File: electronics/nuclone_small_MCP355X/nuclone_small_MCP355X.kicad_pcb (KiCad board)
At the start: 2 copper layers, 50 x 50 mm, 54 parts, among them J3 nuclone_small_left, J4 nuclone_small_right, J5 FTDI_PINS_1X06, J6 DevBoardUartInput

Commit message: WIP schematic, added breadboard, initial placement
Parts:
- added C1: 10n, SquantorRcl:C_0603, F.Cu at (85.0, 81.6)
- added C2: 2.2n, SquantorRcl:C_0603, F.Cu at (87.6, 81.6)
- added C3: 2.2n, SquantorRcl:C_0603, F.Cu at (82.4, 81.6)
- added C5: 1u, SquantorRcl:C_0603, F.Cu at (81.4, 74.8)
- added C6: 1u, SquantorRcl:C_0603, F.Cu at (81.4, 77.5)
- added D2: SD05, SquantorDiodes:SOD-323-nexperia-hand, F.Cu at (76.6, 106.9)
- added D3: SD05, SquantorDiodes:SOD-323-nexperia-hand, F.Cu at (76.6, 108.7)
- added D4: SD05, SquantorDiodes:SOD-323-nexperia-hand, F.Cu at (93.4, 108.7)
- added D5: SD05, SquantorDiodes:SOD-323-nexperia-hand, F.Cu at (93.4, 106.9)
- added J1: Conn_01x04, SquantorConnectors:Header-0254-1X04-H010, F.Cu at (81.2, 88.5)
- added J10: Conn_01x04, SquantorConnectors:Header-0254-1X04-H010, F.Cu at (83.7, 98.6)
- added J11: Conn_01x04, SquantorConnectors:Header-0254-1X04-H010, F.Cu at (86.3, 98.6)
- added J12: Conn_01x04, SquantorConnectors:Header-0254-1X04-H010, F.Cu at (88.8, 98.6)
- added J13: Conn_01x04, Connector_JST:JST_XH_B4B-XH-A_1x04_P2.50mm_Vertical, F.Cu at (81.2, 106.9)
- added J2: Conn_01x04, SquantorConnectors:Header-0254-1X04-H010, F.Cu at (83.7, 88.5)
- added J7: Conn_01x04, SquantorConnectors:Header-0254-1X04-H010, F.Cu at (86.3, 88.5)
- added J8: Conn_01x04, SquantorConnectors:Header-0254-1X04-H010, F.Cu at (88.8, 88.5)
- added J9: Conn_01x04, SquantorConnectors:Header-0254-1X04-H010, F.Cu at (81.2, 98.6)
- added R1: 1K, SquantorRcl:R_0603_hand, F.Cu at (83.7, 81.6)
- added R10: 1K, SquantorRcl:R_0805+0603, F.Cu at (93.3, 89.7)
- added R11: 1K, SquantorRcl:R_0805+0603, F.Cu at (93.0, 92.2)
- added R2: 1K, SquantorRcl:R_0603_hand, F.Cu at (86.3, 81.6)
- added R3: 100, SquantorRcl:R_0603_hand, F.Cu at (81.4, 72.0)
- added R4: 1K, SquantorRcl:R_0805+0603, F.Cu at (78.0, 84.7)
- added R5: 1K, SquantorRcl:R_0805+0603, F.Cu at (78.0, 87.2)
- added R6: 1K, SquantorRcl:R_0805+0603, F.Cu at (78.0, 89.8)
- added R7: 1K, SquantorRcl:R_0805+0603, F.Cu at (78.0, 92.2)
- added R8: 1K, SquantorRcl:R_0805+0603, F.Cu at (93.5, 86.9)
- added R9: 1K, SquantorRcl:R_0805+0603, F.Cu at (93.0, 84.7)
- added TP40: SCK, SquantorTestPoints:TestPoint_hole_H05R10_2side, F.Cu at (87.2, 71.5)
- added TP41: SDO, SquantorTestPoints:TestPoint_hole_H05R10_2side, F.Cu at (85.7, 71.5)
- added TP42: CS, SquantorTestPoints:TestPoint_hole_H05R10_2side, F.Cu at (84.2, 71.5)
- added U1: MCP355X-E_SN, SquantorIC:SOIC-8, F.Cu at (85.0, 76.1)
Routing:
- net /VDD2: track 7.48 -> 29.0 mm
- net /Input2: track 0.00 -> 19.0 mm
- net /Input3: track 0.00 -> 19.0 mm
- net /Input4: track 0.00 -> 15.7 mm
- net /Input1: track 0.00 -> 15.7 mm
- net /V_IN-: track 0.00 -> 11.2 mm
- net /V_IN+: track 0.00 -> 9.83 mm
- net Net-(U1-Vin+): track 0.00 -> 5.08 mm
- net Net-(U1-Vin-): track 0.00 -> 3.74 mm
- net Net-(U1-Vdd): track 0.00 -> 3.27 mm
- net /VREF: track 0.00 -> 3.06 mm
- net /SCK: track 0.00 -> 2.02 mm
- net /CS: track 0.00 -> 1.97 mm
- net /SDO: track 0.00 -> 1.93 mm
- net /VSS: vias 10 -> 15

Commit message: placing and silk placement
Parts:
- moved R9 2.66 mm to (92.1, 87.2)
- moved R8 2.61 mm to (92.1, 84.7)
- moved R10 1.20 mm to (92.1, 89.8)
- moved R11 0.90 mm to (92.1, 92.2)
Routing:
- net /VREF: track 3.06 -> 56.0 mm, vias 0 -> 2
- net /DIV3: track 0.00 -> 7.56 mm
- net /DIV4: track 0.00 -> 7.49 mm
- net /DIV1: track 0.00 -> 7.36 mm
- net /DIV2: track 0.00 -> 7.29 mm
- net /VSS: track 0.00 -> 4.84 mm, vias 15 -> 19

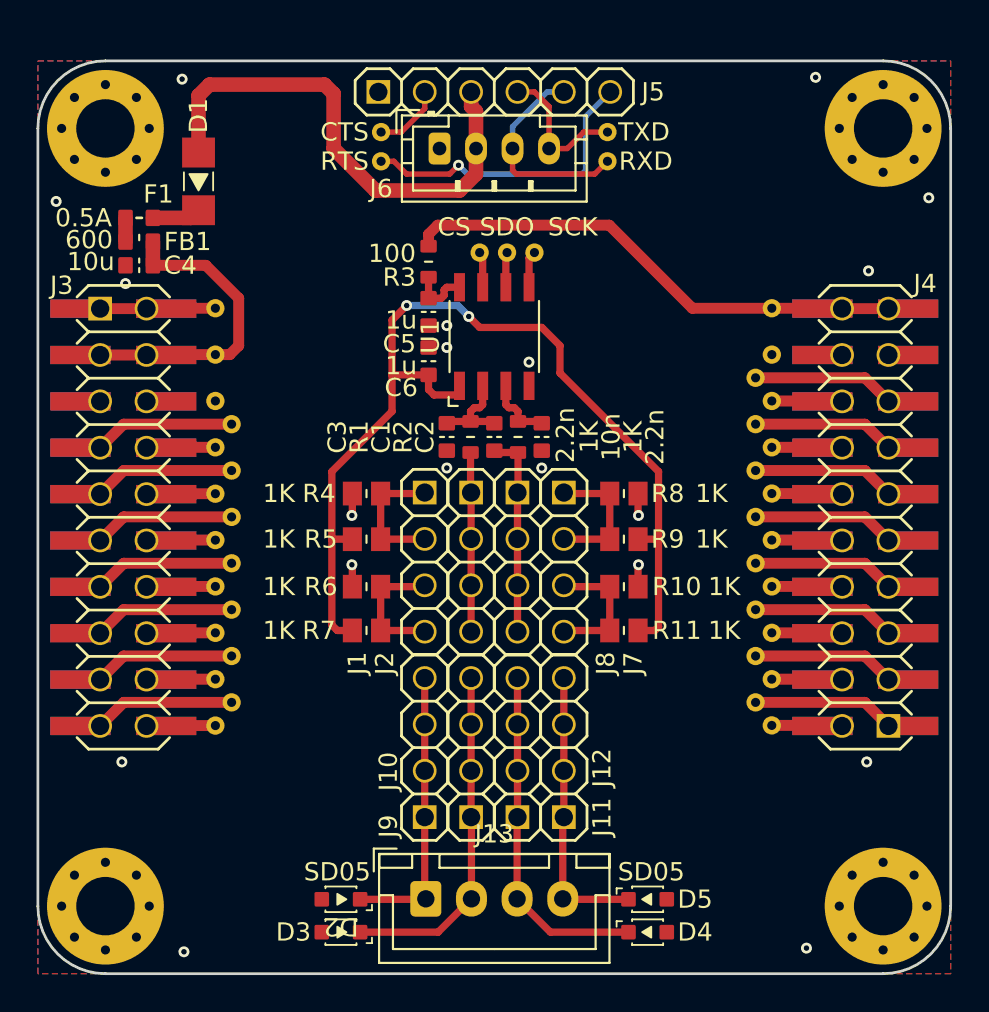
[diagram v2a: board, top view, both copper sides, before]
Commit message: added Voltage reference, placed and routed
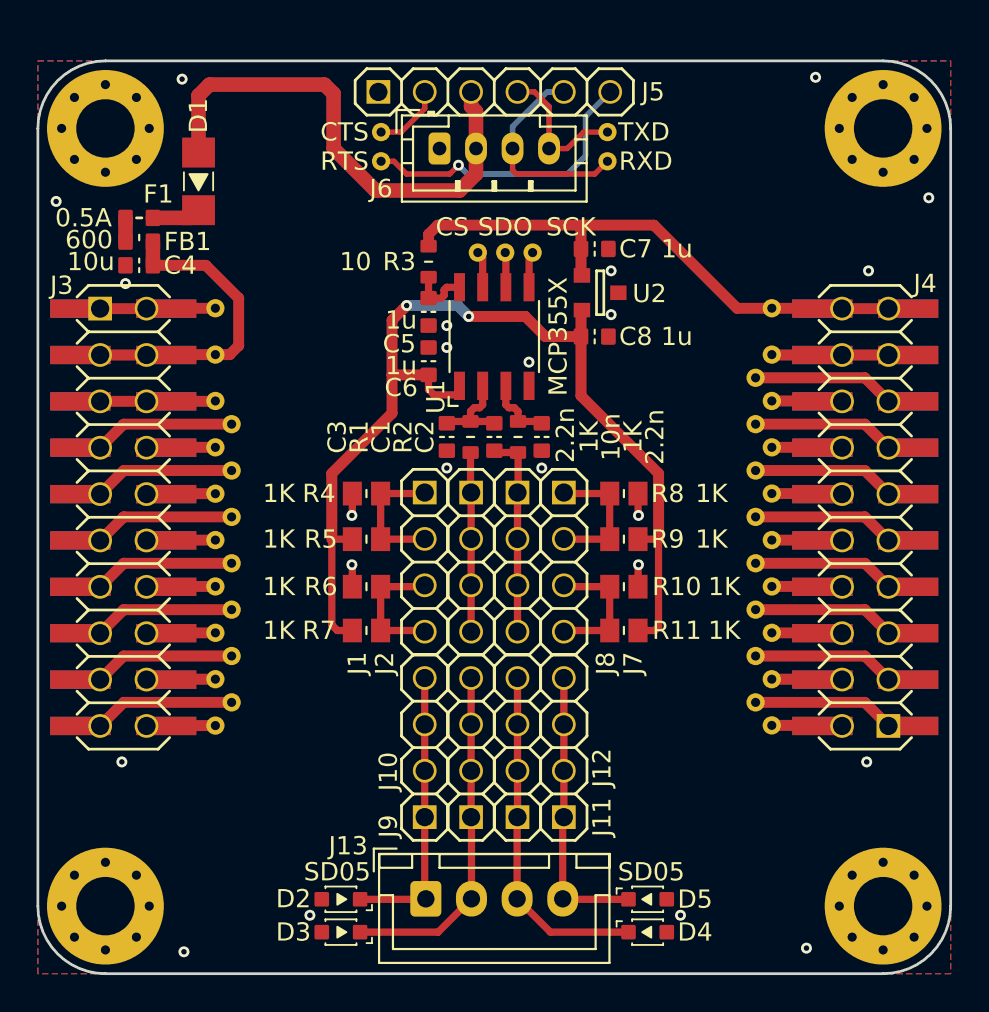
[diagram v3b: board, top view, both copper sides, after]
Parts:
- added C7: 1u, SquantorRcl:C_0603, F.Cu at (90.5, 71.3)
- added C8: 1u, SquantorRcl:C_0603, F.Cu at (90.5, 76.1)
- added U2: reference_sot23-3, SquantorIC:SOT23-3, F.Cu at (90.8, 73.7)
- N2: value V20230714 -> V20230801
- R3: value 100 -> 10
- U1: value MCP355X-E_SN -> MCP355X
- moved TP40 0.10 mm to (87.1, 71.5)
- moved TP41 0.10 mm to (85.6, 71.5)
- moved TP42 0.10 mm to (84.1, 71.5)
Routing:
- net /VSS: track 4.84 -> 18.6 mm, vias 19 -> 23
- net /VDD2: track 29.0 -> 31.8 mm
- net /VREF: track 56.0 -> 58.4 mm

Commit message: reviewed and small modifications
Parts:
- removed TP40: SCK, SquantorTestPoints:TestPoint_hole_H05R10_2side
- removed TP41: SDO, SquantorTestPoints:TestPoint_hole_H05R10_2side
- removed TP42: CS, SquantorTestPoints:TestPoint_hole_H05R10_2side
- added J14: Conn_01x03, SquantorConnectors:Header-0254-1X03-H010, F.Cu at (85.7, 70.8)
- N2: value V20230801 -> V20230915
- moved R3 1.92 mm to (80.2, 70.5)
- moved C7 0.70 mm to (91.2, 71.3)
- moved C8 0.70 mm to (91.2, 76.1)
- moved U2 0.70 mm to (91.5, 73.7)
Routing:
- net Net-(U1-Vdd): track 3.27 -> 5.27 mm
- net /SCK: track 1.98 -> 3.14 mm
- net /CS: track 2.01 -> 3.12 mm
- net /VDD2: track 31.8 -> 32.7 mm
- net /SDO: track 1.91 -> 2.61 mm

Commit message: updated changes and library
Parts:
- removed J14: Conn_01x03, SquantorConnectors:Header-0254-1X03-H010
- removed J5: FTDI_PINS_1X06, SquantorConnectors:Header-0254-1X06-H010
- removed TP36: CTS, SquantorTestPoints:TestPoint_hole_H05R10_2side
- removed TP37: RTS, SquantorTestPoints:TestPoint_hole_H05R10_2side
- removed TP38: TXD, SquantorTestPoints:TestPoint_hole_H05R10_2side
- removed TP39: RXD, SquantorTestPoints:TestPoint_hole_H05R10_2side
- added D6: LED, SquantorDiodes:LED_0603_hand, F.Cu at (71.2, 71.0)
- added J15: Conn_02x03_Odd_Even, SquantorConnectors:Header-0254-2X03-H010, F.Cu at (86.2, 74.4)
- added J16: Conn_02x04_Odd_Even, SquantorConnectors:Header-0254-2X04-H010, F.Cu at (93.4, 66.6)
- added R12: 1K, SquantorRcl:R_0603_hand, F.Cu at (68.3, 70.9)
- J10, J11, J12, J9: footprint SquantorConnectors:Header-0254-1X04-H010 -> SquantorConnectors:Header-0254-1X02-H010
- moved R3 7.12 mm to (80.7, 77.6), turned to 180 degrees
- moved C7 6.50 mm to (91.3, 77.8)
- moved C8 6.50 mm to (91.3, 82.6)
- moved U2 6.50 mm to (91.5, 80.2)
- moved R10 5.04 mm to (93.3, 94.7)
- moved R9 5.04 mm to (93.3, 92.1)
- moved R11 5.04 mm to (93.3, 97.1)
- moved R8 5.04 mm to (93.3, 89.6)
- moved R7 5.02 mm to (76.9, 97.1)
- moved R4 5.01 mm to (76.9, 89.6)
- moved R5 5.01 mm to (76.9, 92.1)
- moved R6 5.01 mm to (76.9, 94.7)
- moved C1 4.89 mm to (85.1, 86.5)
- moved C2 4.89 mm to (87.7, 86.5)
- moved C3 4.89 mm to (82.5, 86.5)
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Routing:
- net /RTS: track 16.4 -> 0.00 mm, vias 1 -> 0
- net /VIN: track 27.7 -> 19.0 mm
- net /Input1: track 15.7 -> 10.8 mm
- net /Input2: track 19.0 -> 14.1 mm
- net /Input4: track 15.7 -> 10.9 mm
- net /Input3: track 19.0 -> 14.1 mm
- net /VSS: track 18.6 -> 13.8 mm, vias 23 -> 22
- net /CTS: track 3.83 -> 0.00 mm
- net /DIV2: track 7.29 -> 9.67 mm
- net /DIV1: track 7.36 -> 9.74 mm
- net /DIV3: track 7.56 -> 9.79 mm
- net /DIV4: track 7.49 -> 9.70 mm
- net /VDD2: track 32.7 -> 34.8 mm, vias 0 -> 2
- net Net-(U1-Vdd): track 5.27 -> 3.43 mm
- net /RXD: track 11.6 -> 10.1 mm
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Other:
- board text added: "CS SDO SCK"
- board text added: "RXD TXD RTS CTS"

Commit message: updated versionnumber
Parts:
- N2: value V20230915 -> V20231203
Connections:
- J16 pad 1: /CTS -> unconnected-(J16-Pin_1-Pad1)
- J16 pad 3: /RTS -> unconnected-(J16-Pin_3-Pad3)
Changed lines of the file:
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@@
   (net 36 "/TXD")
   (net 37 "/RXD")
-  (net 38 "/RTS")
-  (net 39 "/CTS")
+  (net 38 "unconnected-(J16-Pin_1-Pad1)")
+  (net 39 "unconnected-(J16-Pin_3-Pad3)")
   (net 40 "Net-(D1-K)")
   (net 41 "/VIN")
@@
       (stroke (width 0.1) (type solid)) (fill solid) (layer "F.SilkS"))
     (pad "1" thru_hole roundrect (at -3.81 1.27 270) (size 1.4 1.4) (drill 1) (layers "*.Cu" "*.Mask") (roundrect_rratio 0.2)
-      (net 39 "/CTS") (pinfunction "Pin_1") (pintype "passive"))
+      (net 38 "unconnected-(J16-Pin_1-Pad1)") (pinfunction "Pin_1") (pintype "passive+no_connect"))
     (pad "2" thru_hole circle (at -3.81 -1.27) (size 1.4 1.4) (drill 1) (layers "*.Cu" "*.Mask")
       (net 2 "/VSS") (pinfunction "Pin_2") (pintype "passive"))
     (pad "3" thru_hole circle (at -1.27 1.27) (size 1.4 1.4) (drill 1) (layers "*.Cu" "*.Mask")
-      (net 38 "/RTS") (pinfunction "Pin_3") (pintype "passive"))
+      (net 39 "unconnected-(J16-Pin_3-Pad3)") (pinfunction "Pin_3") (pintype "passive+no_connect"))
     (pad "4" thru_hole circle (at -1.27 -1.27 270) (size 1.4 1.4) (drill 1) (layers "*.Cu" "*.Mask")
       (net 2 "/VSS") (pinfunction "Pin_4") (pintype "passive"))
@@
         (effects (font (size 1 1) (thickness 0.15)) (justify mirror))
     )
-    (fp_text value "V20230915" (at 0 0.1) (layer "B.SilkS")
+    (fp_text value "V20231203" (at 0 0.1) (layer "B.SilkS")
         (effects (font (size 0.8 0.8) (thickness 0.15)) (justify mirror))
     )

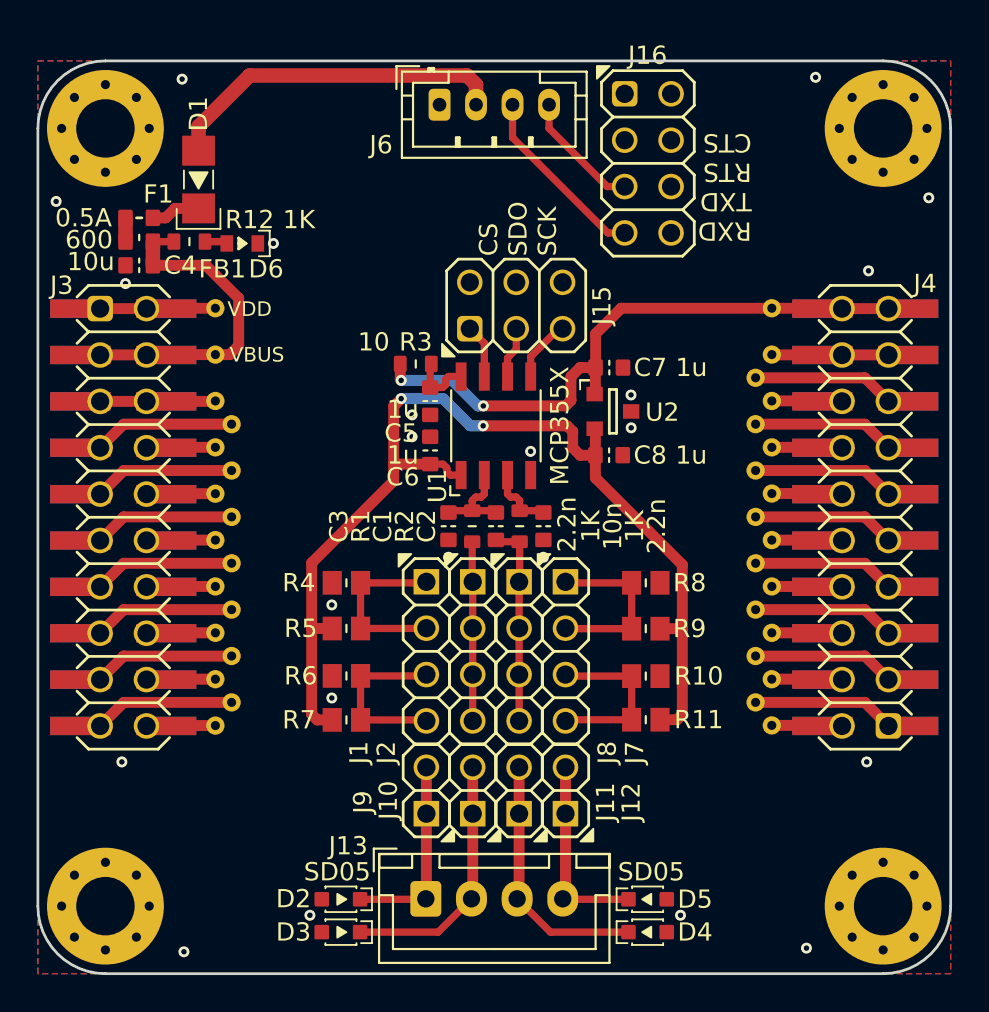
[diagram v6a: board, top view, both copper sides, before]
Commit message: applied aisler simple rules
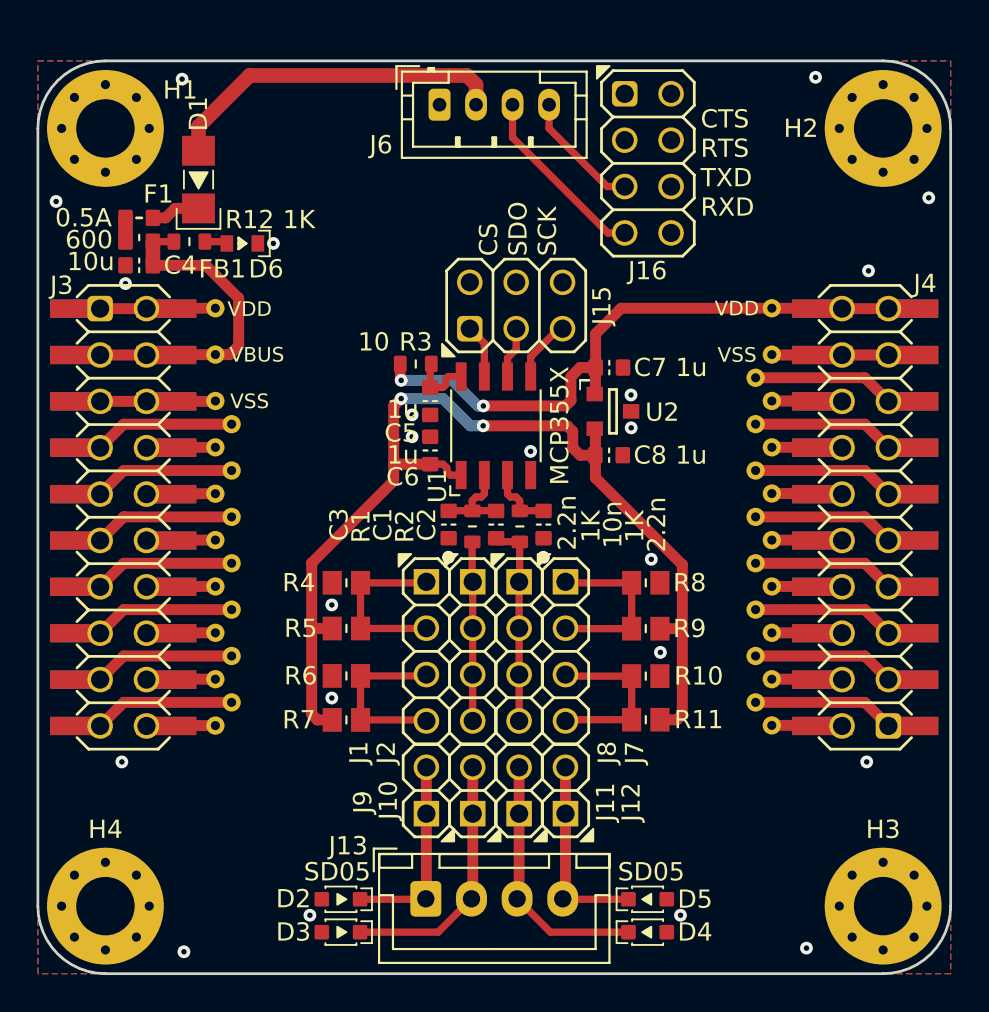
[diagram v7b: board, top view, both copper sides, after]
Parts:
- H1, H2, H3, H4: footprint MountingHole:MountingHole_3.2mm_M3_Pad_Via -> SquantorPcbOutline:MountingHole_3.2mm_M3_Pad_Via
- N2: value V20231203 -> V20231213
- moved C2 0.09 mm to (87.7, 86.4)
- moved C3 0.09 mm to (82.5, 86.4)
- moved C1 0.09 mm to (85.1, 86.4)
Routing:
- net /VSS: vias 22 -> 24
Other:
- board text added: "CTS RTS TXD RXD"
- board text removed: "RXD TXD RTS CTS"
